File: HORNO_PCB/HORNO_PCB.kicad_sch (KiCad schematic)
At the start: 270 parts, among them J0_1 Terminales de tornillo espaci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, J0_10 Terminales de tornillo espaci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, J0_11 Terminales de tornillo espaci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, J0_12 Terminales de tornillo espaci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, J0_13 Terminales de tornillo espaci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, J0_14 Terminales de tornillo espaci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, J0_15 Terminales de tornillo espaci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, J0_16 Terminales de tornillo espaci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, J0_17 Terminales de tornillo espaci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, J0_18 Terminales de tornillo espaci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, J0_19 Terminales de tornillo espaci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, J0_2 Terminales de tornillo espaci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, J0_20 Terminales de tornillo espaci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, J0_21 Terminales de tornillo espaci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, J0_3 Terminales de tornillo espaci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, J0_4 Terminales de tornillo espaci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, J0_5 Terminales de tornillo espaci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, J0_6 Terminales de tornillo espaci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, J0_7 Terminales de tornillo espaci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, J0_8 Terminales de tornillo espaci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, J0_9 Terminales de tornillo espaci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, J1 20 Pin 2.54mm Header Male Bre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, J2 20 Pin 2.54mm Header Male Bre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, J3 20 Pin 2.54mm Header Male Bre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, J4 20 Pin 2.54mm Header Male Bre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, J8 Relay 1, K1 Fujitsu FTR-LYCA005x, K2 Fujitsu FTR-LYCA005x, K3 Fujitsu FTR-LYCA005x, K4 Fujitsu FTR-LYCA005x, K5 SANYOU_SRD_Form_C, Q1 2N2222, Q10 2N2222A, Q11 2N2222A, Q12 2N2222A, Q2 2N2222, Q3 2N2222, Q4 2N2222, Q5 BTA16-800B, Q6 IRG4PF50W, Q7 IRG4PF50W, Q8 2N2222A, Q9 2N2222A, U1 TLP521-1, U10 LM741, U11 LM741, U12 LM741, U13 MOC3021M, U14 TLP521-1, U15 TLP250, U16 TLP521-1, U17 LM741, U18 LM741, U19 TLP250, U2 TLP521-1, U20 L298HN Multiwatt15 H, U21 TLP521-1, U22 TLP521-1, U23 TLP521-1, U24 TLP291, U3 TLP521-1, U4 TLP521-1, U5 TLP521-1, U6 TLP521-1, U7 TLP521-1, U8 TLP521-1, U9 LM741

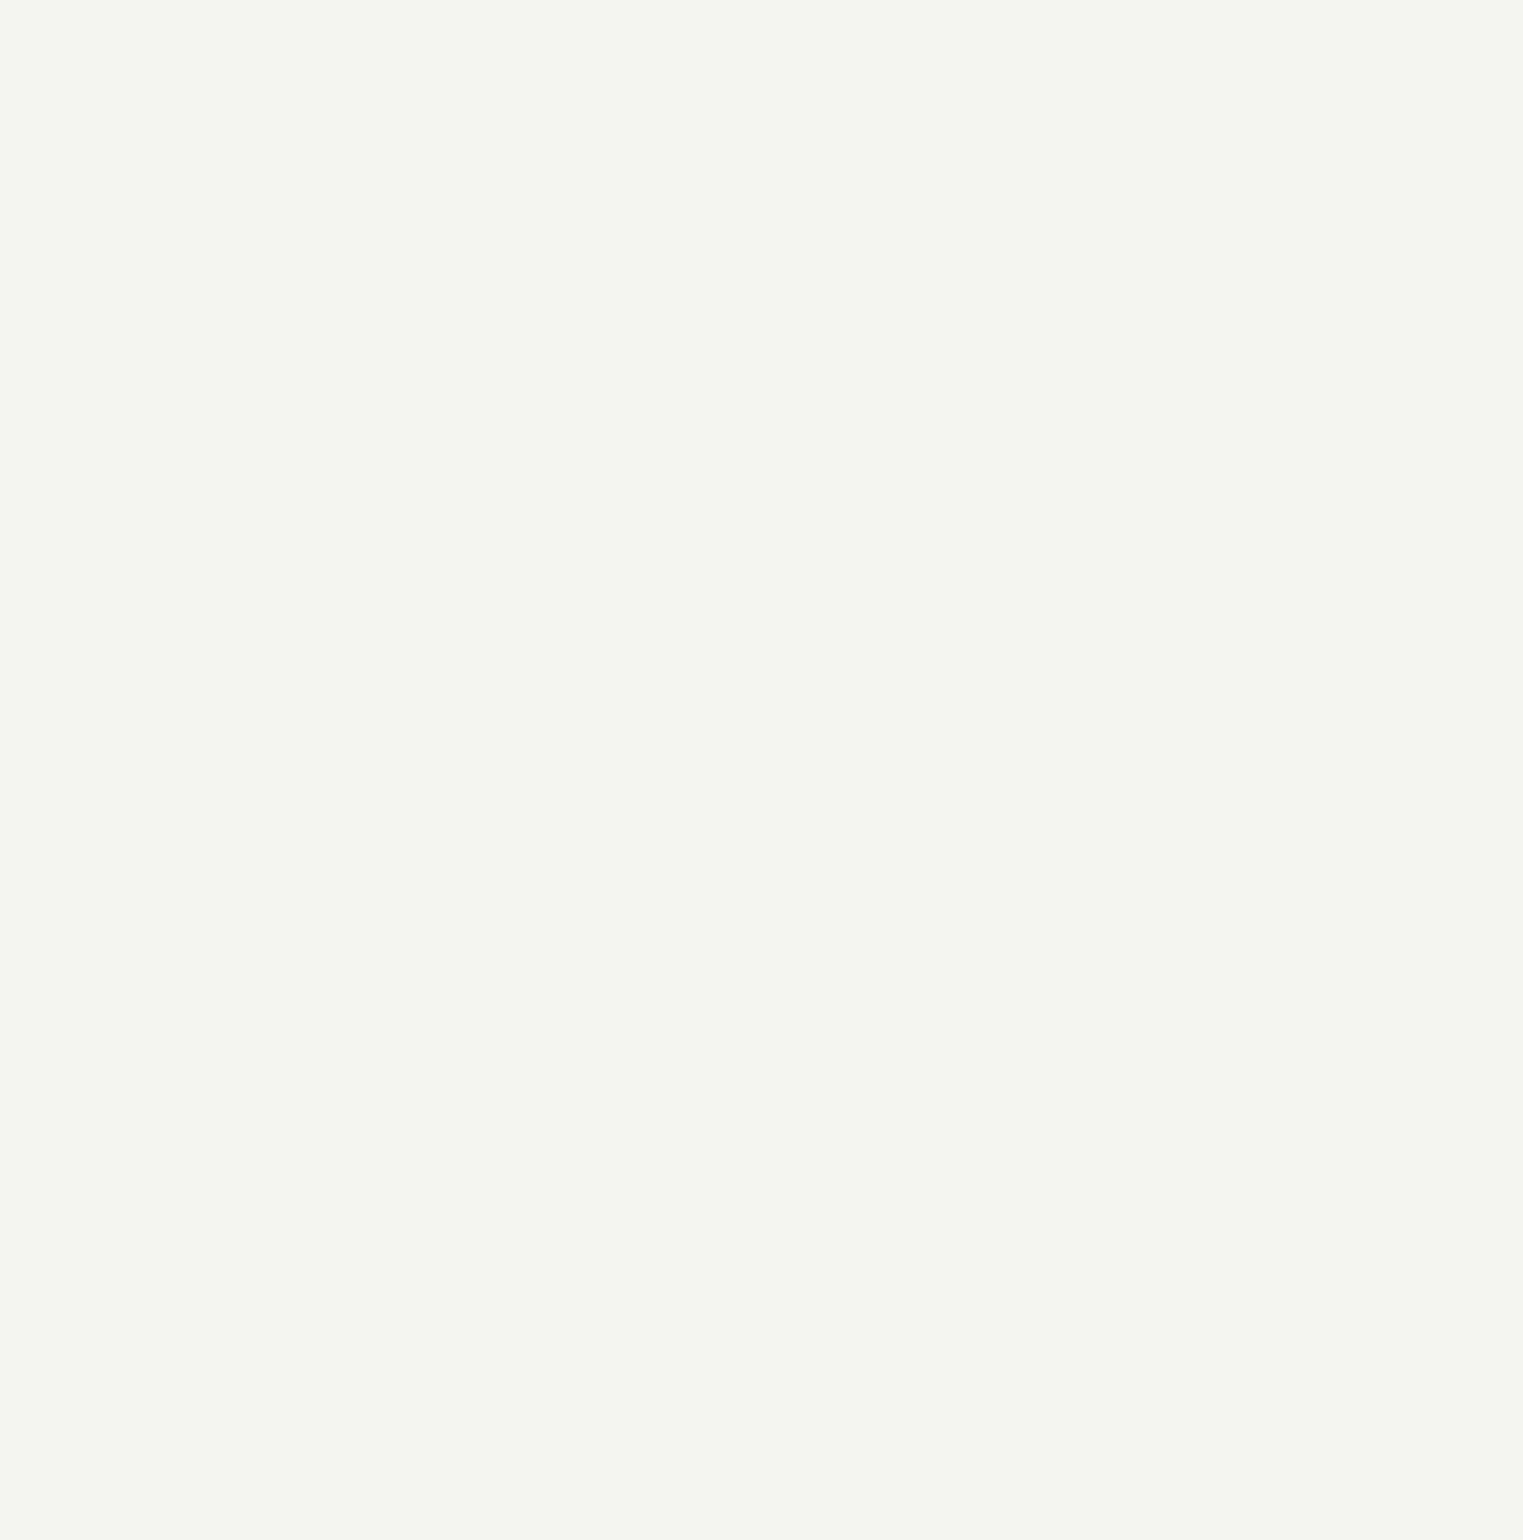
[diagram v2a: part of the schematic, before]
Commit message: Salidas con inversor CMOS 4069 y ULN2803
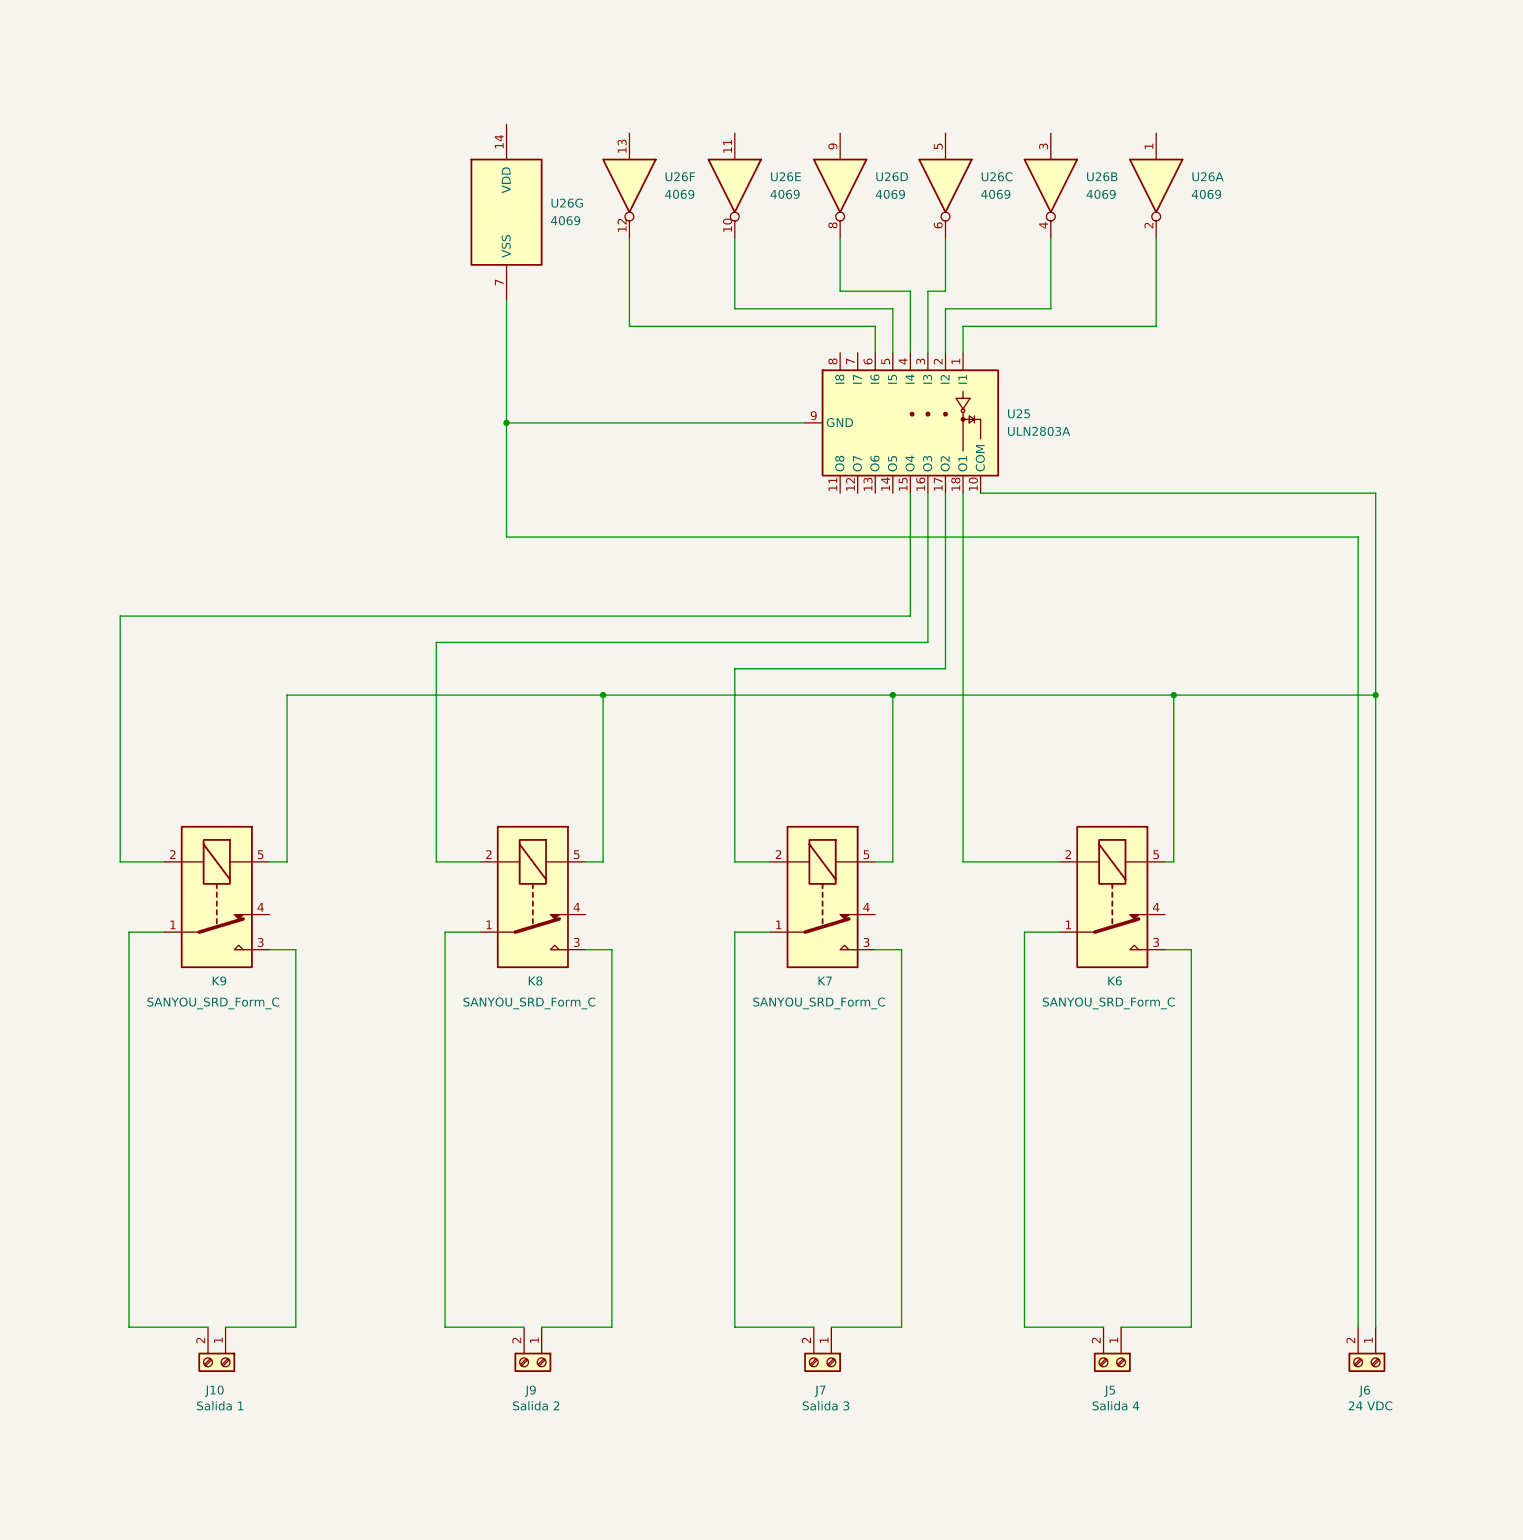
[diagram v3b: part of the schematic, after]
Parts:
- added J10: Salida 1, TerminalBlock_Phoenix:TerminalBlock_Phoenix_MKDS-1,5-2-5.08_1x02_P5.08mm_Horizontal, symbol Connector:Screw_Terminal_01x02
- added J5: Salida 4, TerminalBlock_Phoenix:TerminalBlock_Phoenix_MKDS-1,5-2-5.08_1x02_P5.08mm_Horizontal, symbol Connector:Screw_Terminal_01x02
- added J6: 24 VDC, TerminalBlock_Phoenix:TerminalBlock_Phoenix_MKDS-1,5-2-5.08_1x02_P5.08mm_Horizontal, symbol Connector:Screw_Terminal_01x02
- added J7: Salida 3, TerminalBlock_Phoenix:TerminalBlock_Phoenix_MKDS-1,5-2-5.08_1x02_P5.08mm_Horizontal, symbol Connector:Screw_Terminal_01x02
- added J9: Salida 2, TerminalBlock_Phoenix:TerminalBlock_Phoenix_MKDS-1,5-2-5.08_1x02_P5.08mm_Horizontal, symbol Connector:Screw_Terminal_01x02
- added K6, K7, K8, K9: SANYOU_SRD_Form_C, Relay_THT:Relay_SPDT_SANYOU_SRD_Series_Form_C, symbol Relay:SANYOU_SRD_Form_C
- added U25: ULN2803A, symbol Transistor_Array:ULN2803A
- added U26: 4069, Package_DIP:DIP-14_W7.62mm_LongPads, symbol 4xxx:4069
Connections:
- new net: U25.2 (I2), U26.4
- new net: U25.4 (I4), U26.8
- new net: J10.1 (Pin_1), K9.3
- new net: J10.2 (Pin_2), K9.1
- new net: U25.1 (I1), U26.2
- new net: U25.6 (I6), U26.12
- new net: J9.1 (Pin_1), K8.3
- new net: J9.2 (Pin_2), K8.1
- new net: U25.3 (I3), U26.6
- new net: J5.2 (Pin_2), K6.1
- new net: K6.2, U25.18 (O1)
- new net: J5.1 (Pin_1), K6.3
- new net: J6.1 (Pin_1), K6.5, K7.5, K8.5, K9.5, U25.10 (COM)
- new net: K9.2, U25.15 (O4)
- new net: J6.2 (Pin_2), U25.9 (GND), U26.7 (VSS)
- new net: J7.2 (Pin_2), K7.1
- new net: K7.2, U25.17 (O2)
- new net: J7.1 (Pin_1), K7.3
- new net: U25.5 (I5), U26.10
- new net: K8.2, U25.16 (O3)

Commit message: Interfaces digitales de entrada y salida: corregidas
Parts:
- removed D10: GBU8J, Diode_THT:Diode_Bridge_Vishay_GBU, symbol Diode_Bridge:GBU8J
- removed D11, D12, D13, D9: 1N4007, Diode_THT:D_DO-41_SOD81_P10.16mm_Horizontal, symbol Diode:1N4007
- removed D14: 1N4001, Diode_THT:D_DO-41_SOD81_P10.16mm_Horizontal, symbol Diode:1N4001
- removed J0_11, J0_12, J0_15, J0_17, J0_19, J0_20, J0_21, J0_4, J0_7, J0_8: Terminales de tornillo espaciados en 3.5mm, TerminalBlock_Phoenix:TerminalBlock_Phoenix_PT-1,5-3-3.5-H_1x03_P3.50mm_Horizontal, symbol Connector:Screw_Terminal_01x03
- removed K1, K2, K3, K4: Fujitsu FTR-LYCA005x, Relay_THT:Relay_SPDT_Fujitsu_FTR-LYCA005x_FormC_Vertical, symbol Relay:Fujitsu_FTR-LYCA005x
- removed K5: SANYOU_SRD_Form_C, Relay_THT:Relay_SPDT_SANYOU_SRD_Series_Form_C, symbol Relay:SANYOU_SRD_Form_C
- removed PS5: MEE1S0305SC, Converter_DCDC:Converter_DCDC_Murata_MEE1SxxxxSC_THT, symbol Converter_DCDC:MEE1S0315SC
- removed PX59, PX69: ~, Connector_Wire:SolderWire-0.75sqmm_1x01_D1.25mm_OD2.3mm, symbol Connector:Screw_Terminal_01x01
- removed Q10, Q11, Q12, Q8, Q9: 2N2222A, Package_TO_SOT_THT:TO-92, symbol Transistor_BJT:Q_NPN_EBC
- removed Q5: BTA16-800B, Package_TO_SOT_THT:TO-220-3_Vertical, symbol Triac_Thyristor:BTA16-800B
- removed R12: 330Ω - 1/4 W, Resistor_THT:R_Axial_DIN0207_L6.3mm_D2.5mm_P10.16mm_Horizontal, symbol Device:R_US
- removed R13: Depende de aplicación disparo con triac, Resistor_THT:R_Axial_DIN0309_L9.0mm_D3.2mm_P15.24mm_Horizontal, symbol Device:R_US
- removed R18, R41: 270Ω - 1/4 W, Resistor_THT:R_Axial_DIN0207_L6.3mm_D2.5mm_P10.16mm_Horizontal, symbol Device:R_US
- removed R42, R54, R56, R57, R58, R59, R60, R61: Depende de la tensión aplicada a la bobina del re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, Resistor_THT:R_Axial_DIN0309_L9.0mm_D3.2mm_P15.24mm_Horizontal, symbol Device:R_US
- removed R43, R45, R47, R55: Depende de la tensión aplicada a la bobina del re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, Resistor_THT:R_Axial_DIN0309_L9.0mm_D3.2mm_P12.70mm_Horizontal, symbol Device:R_US
- removed R49: 100 Ω - 1/4 W, Resistor_THT:R_Axial_DIN0207_L6.3mm_D2.5mm_P10.16mm_Horizontal, symbol Device:R_US
- removed R50: 50, Resistor_THT:R_Axial_DIN0309_L9.0mm_D3.2mm_P12.70mm_Horizontal, symbol Device:R_US
- removed R51, R53: 1000, Resistor_THT:R_Axial_DIN0207_L6.3mm_D2.5mm_P10.16mm_Horizontal, symbol Device:R_US
- removed R52: 330, Resistor_THT:R_Axial_DIN0207_L6.3mm_D2.5mm_P10.16mm_Horizontal, symbol Device:R_US
- removed RV1: 10KΩ Bourns 3266W, Potentiometer_THT:Potentiometer_Bourns_3266W_Vertical, symbol Device:R_Potentiometer_US
- removed U13: MOC3021M, Package_DIP:DIP-6_W7.62mm, symbol Relay_SolidState:MOC3021M
- removed U14, U16, U21, U22, U23: TLP521-1, Package_DIP:DIP-4_W7.62mm, symbol Isolator:Optocoupler_DC_PhotoNPN_AKEC
- removed U24: TLP291, Package_SO:SOIC-4_4.55x2.6mm_P1.27mm, symbol Isolator:TLP291
- added D10, D11, D12, D13, D14, D9: LED, LED_THT:LED_D4.0mm, symbol Device:LED
- added J0_22: Terminales de tornillo espaciados en 3.5mm, TerminalBlock_Phoenix:TerminalBlock_Phoenix_PT-1,5-3-3.5-H_1x03_P3.50mm_Horizontal, symbol Connector:Screw_Terminal_01x03
- added J11: Salida 1, TerminalBlock_Phoenix:TerminalBlock_Phoenix_MKDS-1,5-2-5.08_1x02_P5.08mm_Horizontal, symbol Connector:Screw_Terminal_01x02
- added J12: Salida 2, TerminalBlock_Phoenix:TerminalBlock_Phoenix_MKDS-1,5-2-5.08_1x02_P5.08mm_Horizontal, symbol Connector:Screw_Terminal_01x02
- added K1: Relay 1, Relay_THT:Relay_SPDT_SANYOU_SRD_Series_Form_C, symbol Relay:SANYOU_SRD_Form_C
- added K2: Relay 2, Relay_THT:Relay_SPDT_SANYOU_SRD_Series_Form_C, symbol Relay:SANYOU_SRD_Form_C
- added PX56, PX58, PX60, PX61, PX64, PX65, PX68, PX70, PX71: ~, Connector_Wire:SolderWire-0.75sqmm_1x01_D1.25mm_OD2.3mm, symbol Connector:Screw_Terminal_01x01
- J8: value Relay 1 -> 24 VDC
- K6: value SANYOU_SRD_Form_C -> Relay 4
- K7: value SANYOU_SRD_Form_C -> Relay 3
- K8: value SANYOU_SRD_Form_C -> Relay 2
- K9: value SANYOU_SRD_Form_C -> Relay 1
- R1, R2, R3, R4, R5, R6, R7, R8: value 560Ω - 1/4 W -> 270Ω - 1/4 W
- R10, R11, R9: value Depende de aplicación cruce por cero -> 1 kΩ - 1/4 W; footprint Resistor_THT:R_Axial_DIN0411_L9.9mm_D3.6mm_P25.40mm_Horizontal -> Resistor_THT:R_Axial_DIN0207_L6.3mm_D2.5mm_P10.16mm_Horizontal
- R27, R28, R29, R30, R31, R32, R33, R34: value 100 Ω - 1/4 W -> 2.2 KΩ - 1/4 W
- R44, R46, R48: value 270Ω - 1/4 W -> 1 kΩ - 1/4 W
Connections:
- net at PX50.1 (Pin_1), R5.1: now also U5.4; no longer U5.3
- net at U26.3: now also R46.1
- net at R9.1: now also U26.13
- net at R9.2: now also PX54.1 (Pin_1)
- net at U26.9: now also R11.1
- net at PX48.1 (Pin_1), R3.1: now also U3.4; no longer U3.3
- net at R44.1: now also U26.5
- net at C1.2, C10.1, C11.1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: now also J6.2 (Pin_2), U1.3, U2.3, U25.9 (GND), U26.7 (VSS), U3.3, U4.3, U5.3, U6.3, U7.3, U8.3, PX60.1 (Pin_1), PX68.1 (Pin_1); no longer R1.2, R2.2, R3.2, R4.2, R5.2, R6.2, R7.2, R8.2
- net at PX53.1 (Pin_1), R8.1: now also U8.4; no longer U8.3
- net at J8.2 (Pin_2): now also PX61.1 (Pin_1), PX70.1 (Pin_1)
- net at J8.1 (Pin_1): now also PX58.1 (Pin_1), PX65.1 (Pin_1)
- net at U26.1: now also R48.1
- net at PX52.1 (Pin_1), R7.1: now also U7.4; no longer U7.3
- net at PX51.1 (Pin_1), R6.1: now also U6.4; no longer U6.3
- net at R10.1: now also U26.11
- net at K6.2, U25.18 (O1): now also D9.1 (K)
- net at J6.1 (Pin_1), K6.5, K7.5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: now also D10.2 (A), D11.2 (A), D12.2 (A), D13.2 (A), D14.2 (A), D9.2 (A), K1.5, K2.5
- net at K9.2, U25.15 (O4): now also D12.1 (K)
- net at U26.14 (VDD): now also 5Va1.1 (Pin_1), J1.2 (Pin_2), PX71.1 (Pin_1)
- net at PX57.1 (Pin_1): now also R11.2
- net at PX46.1 (Pin_1), R1.1: now also U1.4; no longer U1.3
- net at K7.2, U25.17 (O2): now also D10.1 (K)
- net at R10.2: now also PX56.1 (Pin_1)
- net at PX47.1 (Pin_1), R2.1: now also U2.4; no longer U2.3
- net at PX49.1 (Pin_1), R4.1: now also U4.4; no longer U4.3
- net at 3V3a1.1 (Pin_1), C1.1, J1.3 (Pin_3): now also R1.2, R2.2, R3.2, R4.2, R5.2, R6.2, R7.2, R8.2, PX64.1 (Pin_1)
- net at K8.2, U25.16 (O3): now also D11.1 (K)
- net at U25.13 (O6): now also D14.1 (K), K1.2
- net at U25.14 (O5): now also D13.1 (K), K2.2
- new net: J11.1 (Pin_1), K1.3
- new net: J11.2 (Pin_2), K1.1
- new net: J12.2 (Pin_2), K2.1
- new net: J12.1 (Pin_1), K2.3
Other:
- note added: "24 VDC"
- note added: "3.3 VDC"
- note added: "5 VDC"
- note added: "Fuente step-down"
- moved on the sheet: J10, J5, J6, J7, J9, K6, K7, K8, K9, U25, U26A, U26B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

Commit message: Cambios al esquematico y carpeta con datasheets
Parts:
- removed C10, C11: 100nF, Capacitor_THT:C_Disc_D5.1mm_W3.2mm_P5.00mm, symbol Device:C
- removed J0_16, J0_22: Terminales de tornillo espaciados en 3.5mm, TerminalBlock_Phoenix:TerminalBlock_Phoenix_PT-1,5-3-3.5-H_1x03_P3.50mm_Horizontal, symbol Connector:Screw_Terminal_01x03
- removed U26: 4069, Package_DIP:DIP-14_W7.62mm_LongPads, symbol 4xxx:4069
- added 3V3a2, 3V3b2, 5Va2, 5Vb2, GND4, GND5, GND6, P1, P10, P11, P20, P24, P28, P29, P3, P30, P31, P40, P41, P42, P43, P44, P45, P46, P47, P48, P49, P50, P51, P6, P7, P8, P9, PX59, PX69, PX73, PX74, PX75, PX76, PX77, PX78, PX79, PX81, PX82, PX83, PX84, RST2, RX2, TX2: ~, Connector_Wire:SolderWire-0.75sqmm_1x01_D1.25mm_OD2.3mm, symbol Connector:Screw_Terminal_01x01
- added C12, C7: 100nF, Capacitor_THT:C_Disc_D5.1mm_W3.2mm_P5.00mm, symbol Device:C
- added D15, D16, D17, D18, D19, D20, D21, D22: 1N4001, Diode_THT:D_DO-41_SOD81_P10.16mm_Horizontal, symbol Diode:1N4001
- added J13: 24 VDC, TerminalBlock_Phoenix:TerminalBlock_Phoenix_MKDS-1,5-2-5.08_1x02_P5.08mm_Horizontal, symbol Connector:Screw_Terminal_01x02
- J6: value 24 VDC -> 5 VDC
- U25: value ULN2803A -> UDN2981A; footprint (none) -> Package_DIP:DIP-18_W7.62mm_LongPads
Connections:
- net at C1.2, C2.2, C3.2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: now also U25.10 (GND), C12.2, C7.2, D15.2 (A), D17.2 (A), D18.2 (A), D19.2 (A), PX73.1 (Pin_1), PX77.1 (Pin_1), PX81.1 (Pin_1); no longer J6.2 (Pin_2), U25.9 (GND)
- net at R46.1: now also U25.2 (I2)
- net at U25.4 (I4): now also R11.1
- net at J0_10.3 (Pin_3), U20.13 (OUT3): now also D16.2 (A), D17.1 (K)
- net at J0_10.1 (Pin_1), U20.14 (OUT4): now also D15.1 (K), D20.2 (A)
- net at J0_9.3 (Pin_3), U20.2 (OUT1): now also D19.1 (K), D22.2 (A)
- net at J0_9.1 (Pin_1), U20.3 (OUT2): now also D18.1 (K), D21.2 (A)
- net at U20.4 (Vs): now also C12.1, D16.1 (K), D20.1 (K), D21.1 (K), D22.1 (K), PX79.1 (Pin_1)
- net at U20.9 (Vss): now also C7.1, PX83.1 (Pin_1)
- net at D10.2 (A), D11.2 (A), D12.2 (A)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: now also U25.9 (Vs), PX75.1 (Pin_1); no longer J6.1 (Pin_1), U25.10 (COM)
- net at R48.1: now also U25.1 (I1)
- net at U25.6 (I6): now also R9.1
- net at R44.1: now also U25.3 (I3)
- net at R10.1: now also U25.5 (I5)
- new net: J13.1 (Pin_1), J6.1 (Pin_1), PX69.1 (Pin_1), PX76.1 (Pin_1), PX82.1 (Pin_1)
- new net: J6.2 (Pin_2), PX84.1 (Pin_1)
- new net: J13.2 (Pin_2), PX74.1 (Pin_1), PX78.1 (Pin_1)
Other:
- moved on the sheet: J0_10, J0_9
